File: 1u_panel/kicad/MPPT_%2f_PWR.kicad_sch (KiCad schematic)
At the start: 69 parts, among them J1 SAMTEC-MMS-104-02-X-SHJ, Q1 MOSFET-PCH-SOT23-6, Q2 MOSFET-PCH-SOT23-6, U10 U-TI-TPS63060DCT-BUCKBOOST, U12 LTC4412, U3 LT1618EMSTRPBF, U4 INA226AIDGSR

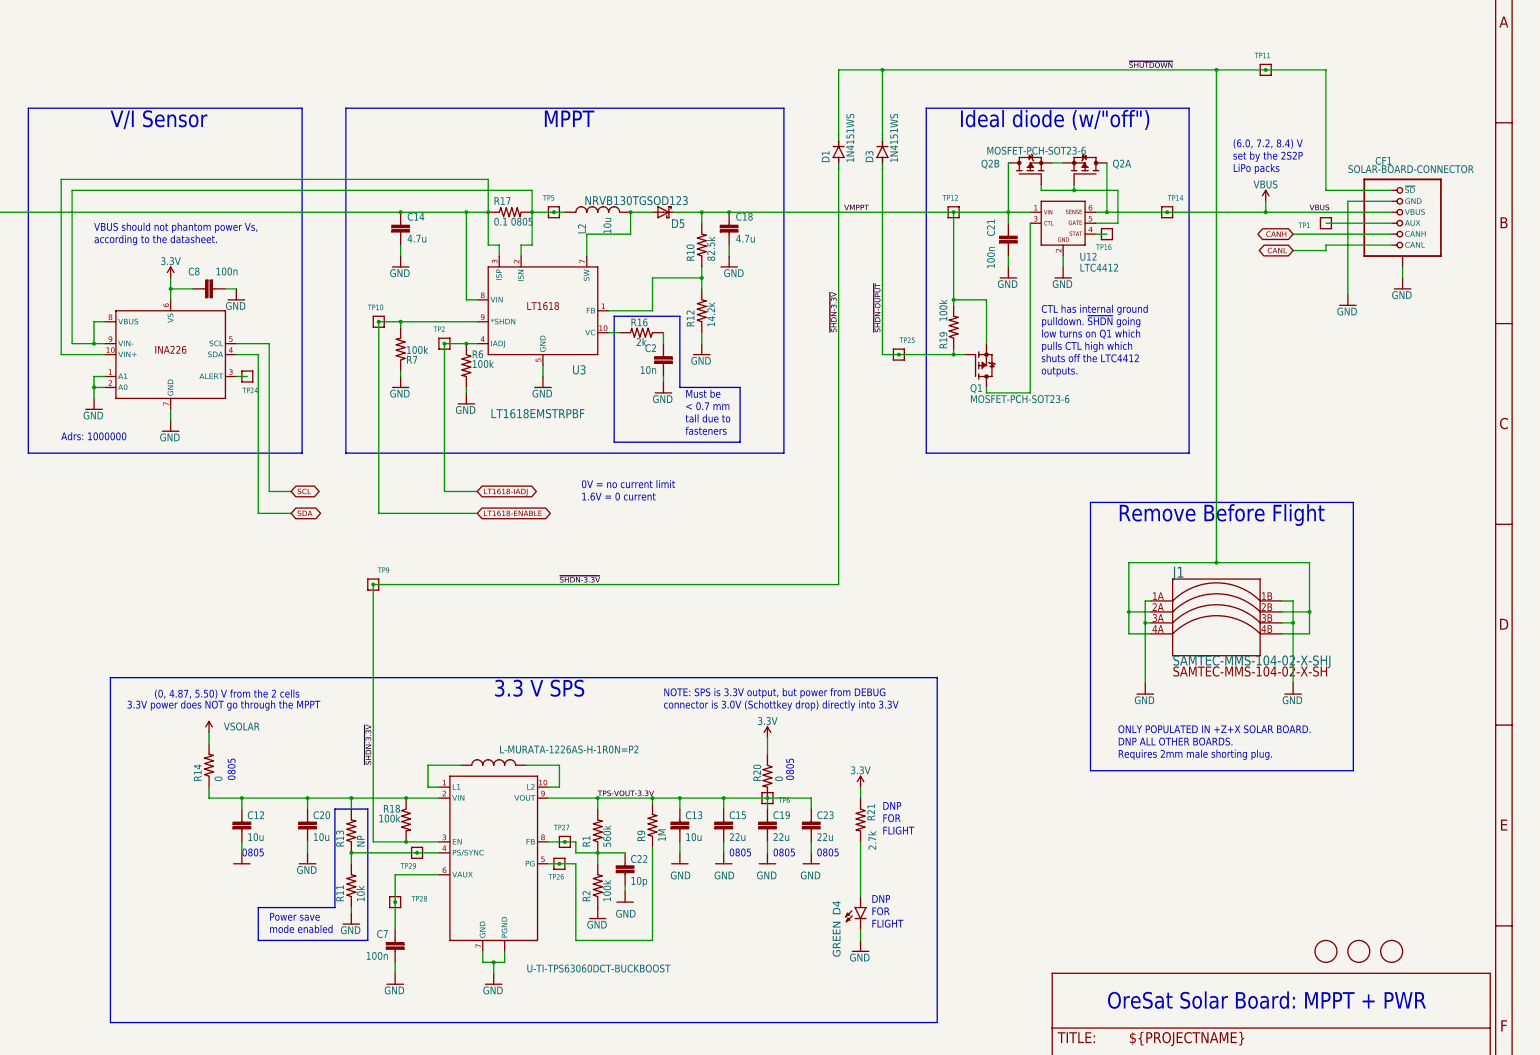
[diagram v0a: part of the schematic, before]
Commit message: Cleaned up schematic; added correct values and part numbers, added datasheet links to important components, imported sch to brd, LOTS of errors to clean up there but it's at synced now.
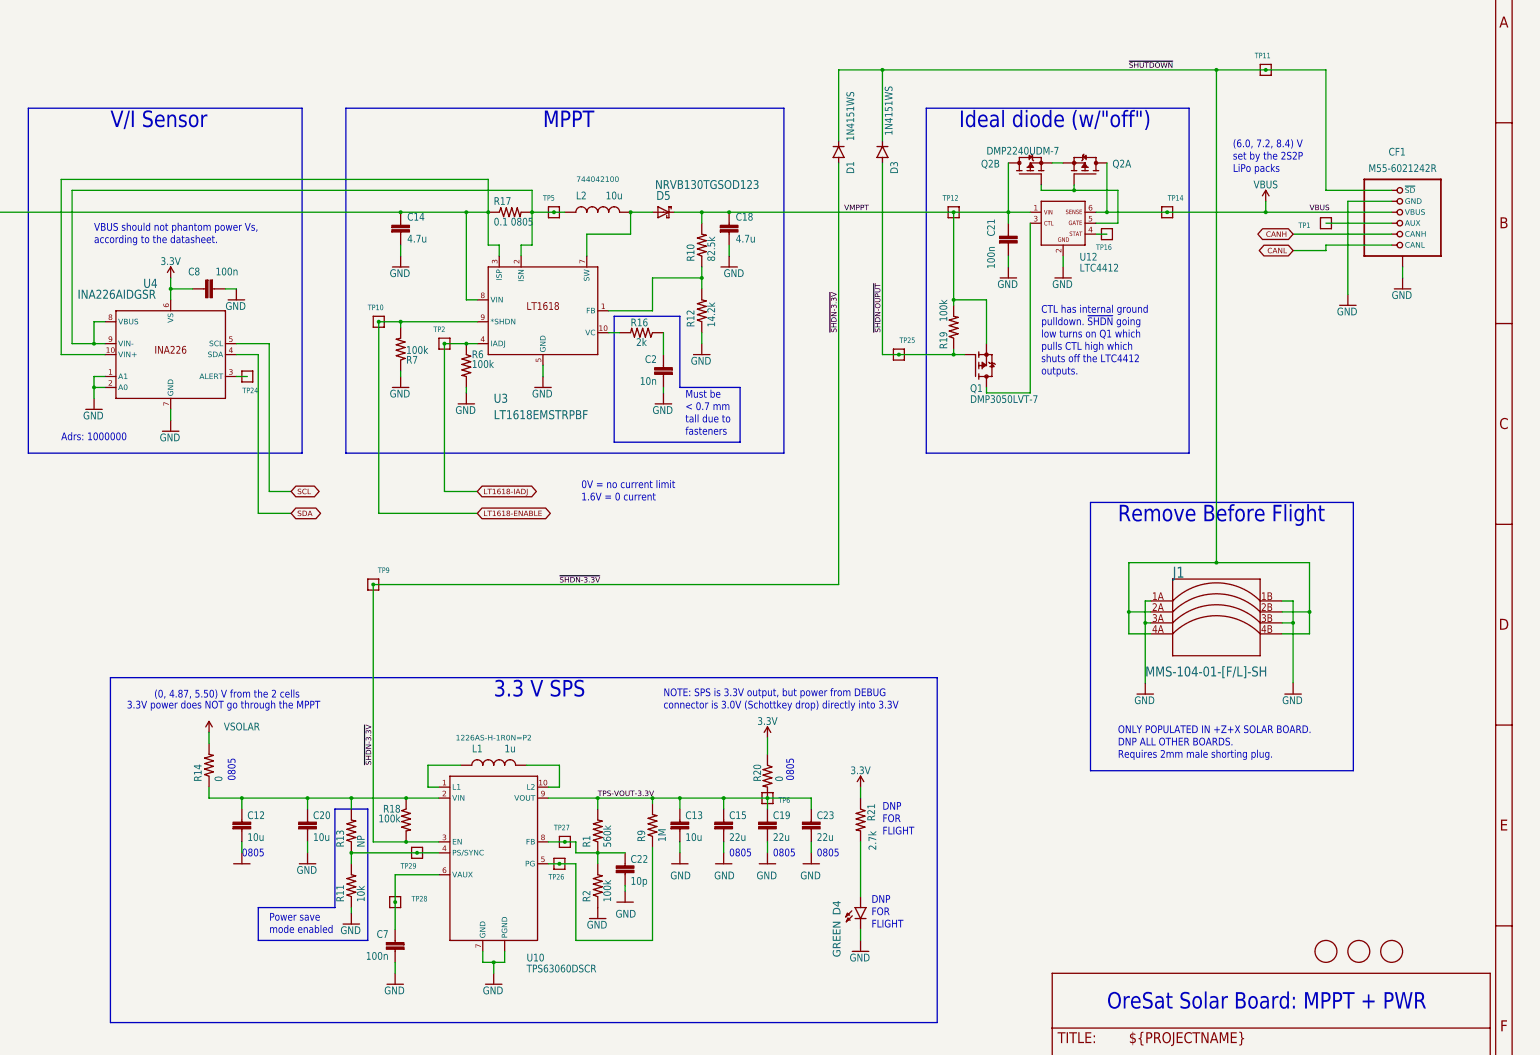
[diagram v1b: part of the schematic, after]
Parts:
- CF1: value SOLAR-BOARD-CONNECTOR -> M55-6021242R
- J1: value SAMTEC-MMS-104-02-X-SHJ -> MMS-104-01-[F/L]-SH
- L1: value L-MURATA-1226AS-H-1R0N=P2 -> 1u; MPN VLS3010CX-1R5M-1 -> 1226AS-H-1R0N=P2
- Q1: value MOSFET-PCH-SOT23-6 -> DMP3050LVT-7
- Q2: value MOSFET-PCH-SOT23-6 -> DMP2240UDM-7
- U10: value U-TI-TPS63060DCT-BUCKBOOST -> TPS63060DSCR
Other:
- moved on the sheet: C2
